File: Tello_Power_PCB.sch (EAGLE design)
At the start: 134 parts, among them CON1 XT30PW-F, CON2 XT30PW-F, CON3 XT30PW-F, CON4 XT30PW-F, CON7 XT60PW-M, J1 PJ-002A, J10 SM02BGHSTBLFSN, J2 1719740002, J3 1719740002, J4 1719740002, J5 1719740002, J6 1719740002, J7 1719740002, J8 1719740002, J9 1719740002, M1 30V, M2 60V, M3 30V, M4 60V, Q1 BSC027N06LS5ATMA1, Q2 BSC027N06LS5ATMA1, Q3 IXTA96P085T, Q7 IXTA96P085T, Q8 IXTA96P085T, Q9 IXTA96P085T, U1 LM3150MH/NOPB, U10 TLV6713DDCTDDC0006A_M, U11 TLV6713DDCTDDC0006A_M, U12 DMN67D8LW-13, U13 MCP1792T-5002H/CB, U14 TLV6713DDCTDDC0006A_M, U2 LM3150MH/NOPB, U3 LTC4357CMS8TRPBF, U4 ADS1015IDGST, U5 DMN67D8LW-13, U6 DMN67D8LW-13, U7 DMN67D8LW-13, U8 LTC4357CMS8TRPBF, U9 TLV6713DDCTDDC0006A_M

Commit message: Organized Schematic
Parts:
- R20, R21: value (none) -> 100K
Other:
- note added: "Battery Input"
- note added: "I²C Address is 1001000"
- note removed: "Default I²C Address = 1001000"
- note removed: "Power Input"

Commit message: Review Finished
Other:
- note removed: "ADD BULK CAPACITANCE HERE"
- note removed: "Bulk capacitance shown on the other Reg. circuit"
- moved on the sheet: C10, C11, C12, C13, C14, C15, C16, C17, C18, C19, C20, C21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

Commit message: Added mfg files and renders
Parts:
- C1, C2, C29, C36, C38: device rcl:C-EUC1206 -> Tello_Power_PCB:RCL_C-EUC1206
- C10, C9: device 12v- LM3150:C2012X5R1V156M125AC -> Tello_Power_PCB:12V--LM3150_C2012X5R1V156M125AC
- C11: device 12v- LM3150:C1005X5R1H104K050BB -> Tello_Power_PCB:12V--LM3150_C1005X5R1H104K050BB
- C12, C24: device CGA4F2C0G1H153J085AA:CGA4F2C0G1H153J085AA -> Tello_Power_PCB:CGA4F2C0G1H153J085AA_CGA4F2C0G1H153J085AA
- C13: device 12v- LM3150:EMK212BJ225KG-T -> Tello_Power_PCB:12V--LM3150_EMK212BJ225KG-T:1
- C14: device 12v- LM3150:ECPU1C474MA5 -> Tello_Power_PCB:12V--LM3150_ECPU1C474MA5:1
- C15: device 12v- LM3150:C0805C301J5GACTU -> Tello_Power_PCB:12V--LM3150_C0805C301J5GACTU
- C16: device 12v- LM3150:PCV1E330MCL1GS -> Tello_Power_PCB:12V--LM3150_PCV1E330MCL1GS
- C17, C18, C19, C4, C5, C6: value PCR1H820MCL1GS -> PCR1H820MCL1GS_PCR1H820MCL1GS; device PCR1H820MCL1GS:PCR1H820MCL1GS -> Tello_Power_PCB:PCR1H820MCL1GS_PCR1H820MCL1GS
- C20: device 5v-LM3150MH:293D335X9035C2TE3 -> Tello_Power_PCB:5V-LM3150MH_293D335X9035C2TE3
- C21, C22: device 5v-LM3150MH:C2012X5R1V106K085AC -> Tello_Power_PCB:5V-LM3150MH_C2012X5R1V106K085AC
- C23: device 5v-LM3150MH:CGA3E2X7R1H104K080AA -> Tello_Power_PCB:5V-LM3150MH_CGA3E2X7R1H104K080AA
- C25: device 5v-LM3150MH:EMK212BJ225KG-T -> Tello_Power_PCB:5V-LM3150MH_EMK212BJ225KG-T
- C26: device 5v-LM3150MH:ECPU1C474MA5 -> Tello_Power_PCB:5V-LM3150MH_ECPU1C474MA5
- C27: device 5v-LM3150MH:CL21C620JBANNNC -> Tello_Power_PCB:5V-LM3150MH_CL21C620JBANNNC
- C28: device 5v-LM3150MH:CUSTOM_CAP -> Tello_Power_PCB:5V-LM3150MH_CUSTOM_CAP
- C3, C30, C37: device rcl:C-EUC0603 -> Tello_Power_PCB:RCL_C-EUC0603
- C31, C32, C33, C34, C35: value 227AVG050MGBJ -> 227AVG050MGBJ_227AVG050MGBJ; device 227AVG050MGBJ:227AVG050MGBJ -> Tello_Power_PCB:227AVG050MGBJ_227AVG050MGBJ
- C39: device microbuilder:CAP_CERAMIC0603 -> Tello_Power_PCB:MICROBUILDER_CAP_CERAMIC0603
- C40, C41: device rcl:C-EUC1210 -> Tello_Power_PCB:RCL_C-EUC1210
- C7, C8: device 12v- LM3150:TPSB475K035R0700 -> Tello_Power_PCB:12V--LM3150_TPSB475K035R0700
- CON1, CON2, CON3, CON4: value XT30PW-F -> AMASS_XT30PW-F; device amass:XT30PW-F -> Tello_Power_PCB:AMASS_XT30PW-F
- CON7: value XT60PW-M -> AMASS_XT60PW-M; device amass:XT60PW-M -> Tello_Power_PCB:AMASS_XT60PW-M
- CR1, CR2: value STPS1150A -> STPS1150A_STPS1150A; device STPS1150A:STPS1150A -> Tello_Power_PCB:STPS1150A_STPS1150A
- J1: value PJ-002A -> PJ-002A_PJ-002A; device PJ-002A:PJ-002A -> Tello_Power_PCB:PJ-002A_PJ-002A
- J10: value SM02BGHSTBLFSN -> SM02B-GHS-TB_SM02BGHSTBLFSN; device SM02B-GHS-TB:SM02BGHSTBLFSN -> Tello_Power_PCB:SM02B-GHS-TB_SM02BGHSTBLFSN
- J2, J3, J4, J5, J6, J7, J8, J9: value 1719740002 -> 1719740002_1719740002; device 1719740002:1719740002 -> Tello_Power_PCB:1719740002_1719740002
- JP1: device pinhead:PINHD-2X6 -> Tello_Power_PCB:PINHEAD_PINHD-2X6
- JP2: value JUMPER-SMT_2_NC_PASTE_NO-SILK -> SPARKFUN-JUMPERS_JUMPER-SMT_2_NC_PASTE_NO-SILK; device SparkFun-Jumpers:JUMPER-SMT_2_NC_PASTE_NO-SILK -> Tello_Power_PCB:SPARKFUN-JUMPERS_JUMPER-SMT_2_NC_PASTE_NO-SILK
- L1: device 12v- LM3150:74437358082 -> Tello_Power_PCB:12V--LM3150_74437358082
- L2: device 5v-LM3150MH:XAL5030-222MEB -> Tello_Power_PCB:5V-LM3150MH_XAL5030-222MEB
- L3: device XAL4030-332MEB:XAL4030-332MEB -> Tello_Power_PCB:XAL4030-332MEB_XAL4030-332MEB
- L4: device 5v-LM3150MH:NPI43C3R9MTRF -> Tello_Power_PCB:5V-LM3150MH_NPI43C3R9MTRF
- LED1, LED2, LED3, LED4: device led:LEDCHIP-LED0603 -> Tello_Power_PCB:LED_LEDCHIP-LED0603
- M1: device 12v- LM3150:CSD17579Q5A -> Tello_Power_PCB:12V--LM3150_CSD17579Q5A:1
- M2: device 12v- LM3150:CSD18537NQ5A -> Tello_Power_PCB:12V--LM3150_CSD18537NQ5A:1
- M3: device 5v-LM3150MH:CSD17579Q5A -> Tello_Power_PCB:5V-LM3150MH_CSD17579Q5A
- M4: device 5v-LM3150MH:CSD18537NQ5A -> Tello_Power_PCB:5V-LM3150MH_CSD18537NQ5A
- Q1, Q2: value BSC027N06LS5ATMA1 -> BSC027N06LS5ATMA1_BSC027N06LS5ATMA1; device BSC027N06LS5ATMA1:BSC027N06LS5ATMA1 -> Tello_Power_PCB:BSC027N06LS5ATMA1_BSC027N06LS5ATMA1
- Q3, Q7, Q8, Q9: value IXTA96P085T -> IXTA96P085T_IXTA96P085T; device IXTA96P085T:IXTA96P085T -> Tello_Power_PCB:IXTA96P085T_IXTA96P085T
- R1: device 12v- LM3150:CRCW04021R00FKED -> Tello_Power_PCB:12V--LM3150_CRCW04021R00FKED
- R10: device 5v-LM3150MH:CRCW080510K0FKEA -> Tello_Power_PCB:5V-LM3150MH_CRCW080510K0FKEA
- R11: device rcl:R-US_R0805 -> Tello_Power_PCB:RCL_R-US_R0805
- R12, R13, R14, R15, R16, R19, R20, R21, R22, R25, R27, R28, R29, R30, R38, R39, R40, R41, R42, R5: device rcl:R-US_R0603 -> Tello_Power_PCB:RCL_R-US_R0603
- R17, R18, R4: value 68XR10KLF -> 68XR10KLF_68XR10KLF; device 68XR10KLF:68XR10KLF -> Tello_Power_PCB:68XR10KLF_68XR10KLF
- R2: device 12v- LM3150:ERJ-6ENF3323V -> Tello_Power_PCB:12V--LM3150_ERJ-6ENF3323V
- R23, R24, R26, R31, R32, R33, R34, R35, R36, R37: device microbuilder:RESISTOR0603 -> Tello_Power_PCB:MICROBUILDER_RESISTOR0603
- R3: device 12v- LM3150:ERJ-6ENF1371V -> Tello_Power_PCB:12V--LM3150_ERJ-6ENF1371V
- R6: device 5v-LM3150MH:ERJ-3RSFR10V -> Tello_Power_PCB:5V-LM3150MH_ERJ-3RSFR10V
- R7: device 5v-LM3150MH:ERJ-6ENF5112V -> Tello_Power_PCB:5V-LM3150MH_ERJ-6ENF5112V
- R8: device 5v-LM3150MH:ERJ-6ENF1581V -> Tello_Power_PCB:5V-LM3150MH_ERJ-6ENF1581V
- R9: device 5v-LM3150MH:CRCW080573K2FKEA -> Tello_Power_PCB:5V-LM3150MH_CRCW080573K2FKEA
- U1, U2: value LM3150MH/NOPB -> 5V-LM3150MH_LM3150MH/NOPB; device 5v-LM3150MH:LM3150MH/NOPB -> Tello_Power_PCB:5V-LM3150MH_LM3150MH/NOPB
- U10, U11, U14, U9: value TLV6713DDCTDDC0006A_M -> TLV6713DDC_TLV6713DDCTDDC0006A_M; device TLV6713DDC:TLV6713DDCTDDC0006A_M -> Tello_Power_PCB:TLV6713DDC_TLV6713DDCTDDC0006A_M
- U12, U5, U6, U7: value DMN67D8LW-13 -> DMN67D8LW-13_DMN67D8LW-13; device DMN67D8LW-13:DMN67D8LW-13 -> Tello_Power_PCB:DMN67D8LW-13_DMN67D8LW-13
- U13: value MCP1792T-5002H/CB -> MCP1792T-5002H_MCP1792T-5002H/CB; device MCP1792T-5002H:MCP1792T-5002H/CB -> Tello_Power_PCB:MCP1792T-5002H_MCP1792T-5002H/CB
- U3, U8: value LTC4357CMS8TRPBF -> LTC4357_LTC4357CMS8TRPBF; device LTC4357:LTC4357CMS8TRPBF -> Tello_Power_PCB:LTC4357_LTC4357CMS8TRPBF
- U4: device microbuilder:ADC_ADS1015 -> Tello_Power_PCB:MICROBUILDER_ADC_ADS1015

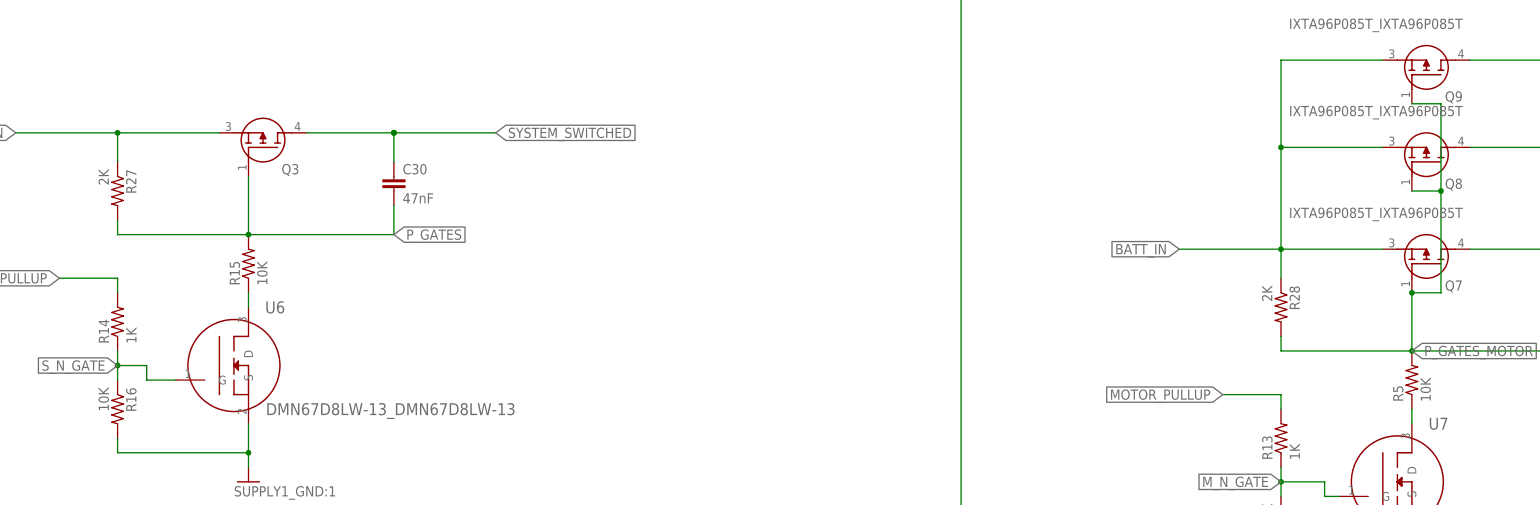
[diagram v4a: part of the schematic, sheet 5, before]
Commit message: updated readme photos
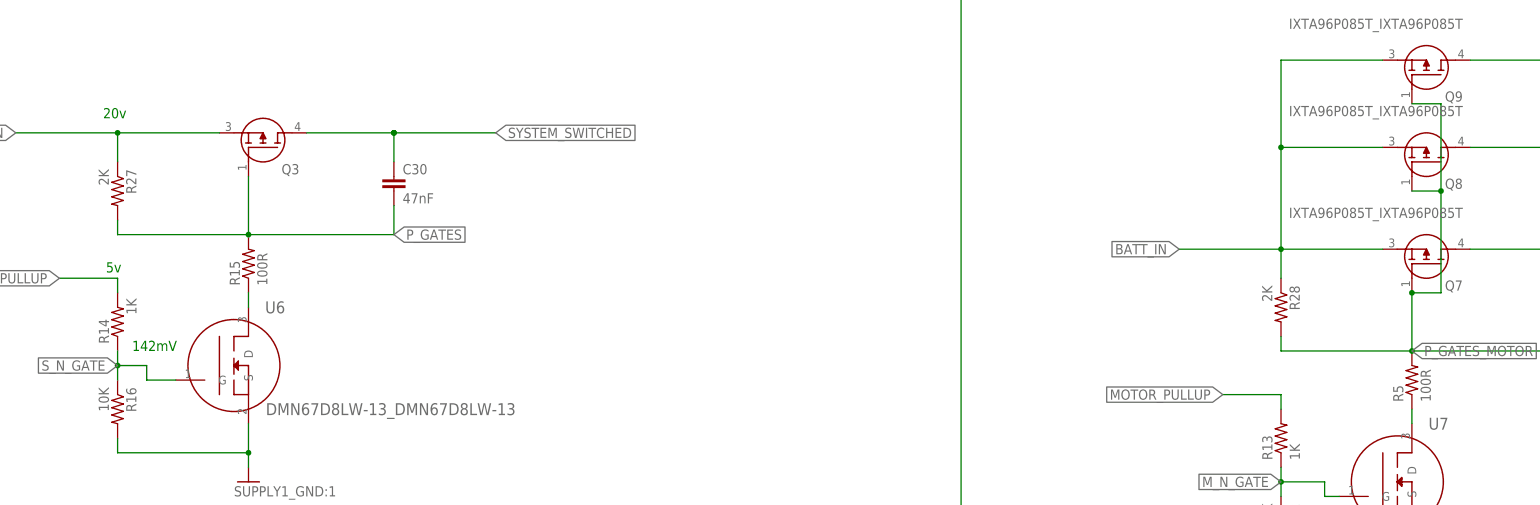
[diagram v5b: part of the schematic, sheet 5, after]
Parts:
- R15, R5: value 10K -> 100R
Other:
- note added: "142mV"
- note added: "20v"
- note added: "3.89v?"
- note added: "4.77"
- note added: "5.24v"
- note added: "5v"
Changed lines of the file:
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@@
 <part name="Q3" library="Tello_Power_PCB" library_urn="urn:adsk.eagle:library:37573195" deviceset="IXTA96P085T_IXTA96P085T" device="" package3d_urn="urn:adsk.eagle:package:37573289/3"/>
 <part name="R27" library="Tello_Power_PCB" library_urn="urn:adsk.eagle:library:37573195" deviceset="RCL_R-US_" device="R0603" package3d_urn="urn:adsk.eagle:package:37573323/1" value="2K"/>
-<part name="R15" library="Tello_Power_PCB" library_urn="urn:adsk.eagle:library:37573195" deviceset="RCL_R-US_" device="R0603" package3d_urn="urn:adsk.eagle:package:37573323/1" value="10K"/>
+<part name="R15" library="Tello_Power_PCB" library_urn="urn:adsk.eagle:library:37573195" deviceset="RCL_R-US_" device="R0603" package3d_urn="urn:adsk.eagle:package:37573323/1" value="100R"/>
 <part name="GND14" library="Tello_Power_PCB" library_urn="urn:adsk.eagle:library:37573195" deviceset="SUPPLY1_GND*?:1" device=""/>
 <part name="R16" library="Tello_Power_PCB" library_urn="urn:adsk.eagle:library:37573195" deviceset="RCL_R-US_" device="R0603" package3d_urn="urn:adsk.eagle:package:37573323/1" value="10K"/>
@@
 <part name="Q9" library="Tello_Power_PCB" library_urn="urn:adsk.eagle:library:37573195" deviceset="IXTA96P085T_IXTA96P085T" device="" package3d_urn="urn:adsk.eagle:package:37573289/3"/>
 <part name="C3" library="Tello_Power_PCB" library_urn="urn:adsk.eagle:library:37573195" deviceset="RCL_C-EU" device="C0603" package3d_urn="urn:adsk.eagle:package:37573320/1" value="47nF"/>
-<part name="R5" library="Tello_Power_PCB" library_urn="urn:adsk.eagle:library:37573195" deviceset="RCL_R-US_" device="R0603" package3d_urn="urn:adsk.eagle:package:37573323/1" value="10K"/>
+<part name="R5" library="Tello_Power_PCB" library_urn="urn:adsk.eagle:library:37573195" deviceset="RCL_R-US_" device="R0603" package3d_urn="urn:adsk.eagle:package:37573323/1" value="100R"/>
 <part name="FRAME11" library="Tello_Power_PCB" library_urn="urn:adsk.eagle:library:37573195" deviceset="FRAMES_FRAME_A_L" device=""/>
 <part name="FRAME12" library="Tello_Power_PCB" library_urn="urn:adsk.eagle:library:37573195" deviceset="FRAMES_FRAME_B_L" device=""/>
@@
 <text x="233.934" y="187.96" size="12.7" layer="91">Motor High Side Switch</text>
 <text x="233.934" y="172.72" size="7.62" layer="91">With Inrush Current Limiter</text>
+<text x="66.04" y="144.78" size="1.778" layer="91">20v</text>
+<text x="71.12" y="104.14" size="1.778" layer="91">142mV</text>
+<text x="66.548" y="117.856" size="1.778" layer="91">5v</text>
 </plain>
 <instances>
@@
 <instance part="R14" gate="G$1" x="68.58" y="109.22" smashed="yes" rot="R90">
 <attribute name="NAME" x="67.0814" y="105.41" size="1.778" layer="95" rot="R90"/>
-<attribute name="VALUE" x="71.882" y="105.41" size="1.778" layer="96" rot="R90"/>
+<attribute name="VALUE" x="71.882" y="110.49" size="1.778" layer="96" rot="R90"/>
 </instance>
 <instance part="Q7" gate="G$1" x="294.64" y="114.3" smashed="yes" rot="MR90">
@@
 <text x="15.24" y="256.54" size="6.35" layer="91">Under- Voltage Protection Circuitry</text>
 <text x="261.62" y="157.48" size="2.54" layer="91">30 Second Filter Circuit</text>
+<text x="312.42" y="91.44" size="1.778" layer="91">5v</text>
+<text x="287.02" y="78.74" size="1.778" layer="91">3.89v?</text>
+<text x="233.68" y="91.44" size="1.778" layer="91">5.24v</text>
+<text x="322.58" y="83.82" size="1.778" layer="91">4.77</text>
 </plain>
 <instances>

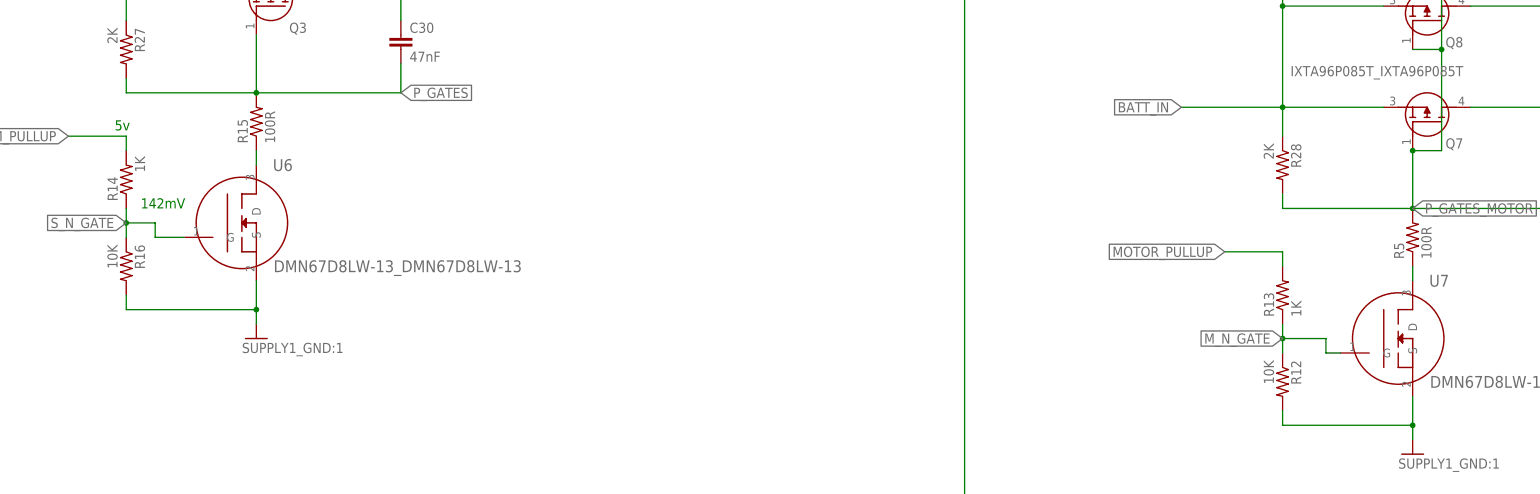
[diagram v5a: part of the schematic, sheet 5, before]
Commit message: updated high side switch resistors
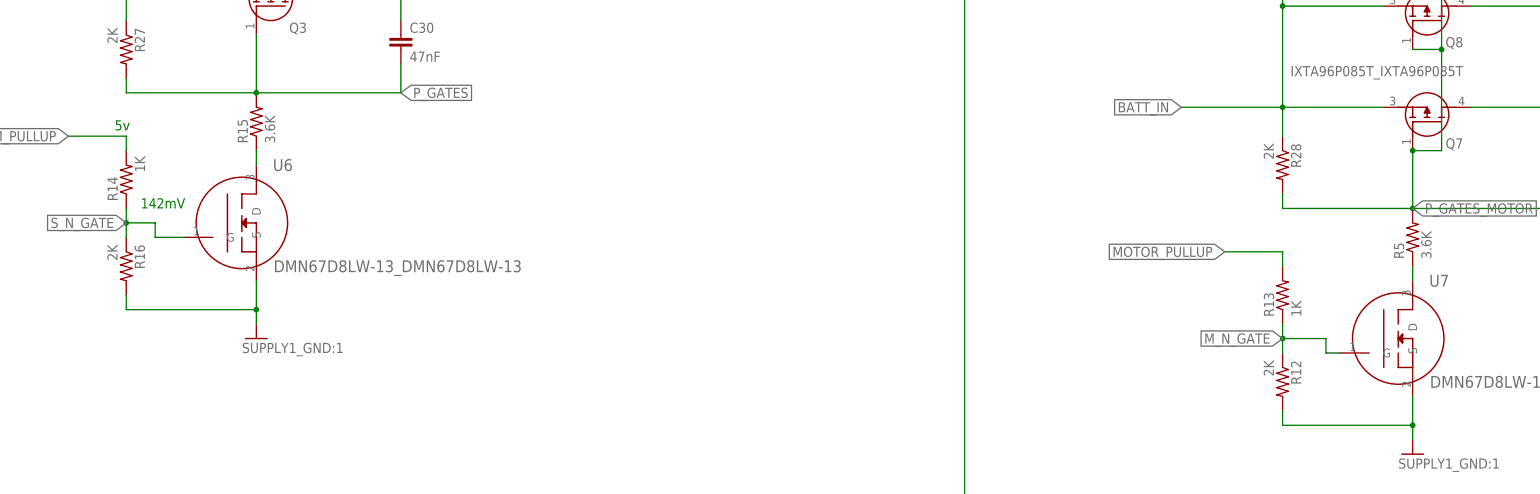
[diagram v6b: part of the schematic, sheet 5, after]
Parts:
- R12, R16: value 10K -> 2K
- R15, R5: value 100R -> 3.6K
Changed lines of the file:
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@@
 <part name="Q3" library="Tello_Power_PCB" library_urn="urn:adsk.eagle:library:37573195" deviceset="IXTA96P085T_IXTA96P085T" device="" package3d_urn="urn:adsk.eagle:package:37573289/3"/>
 <part name="R27" library="Tello_Power_PCB" library_urn="urn:adsk.eagle:library:37573195" deviceset="RCL_R-US_" device="R0603" package3d_urn="urn:adsk.eagle:package:37573323/1" value="2K"/>
-<part name="R15" library="Tello_Power_PCB" library_urn="urn:adsk.eagle:library:37573195" deviceset="RCL_R-US_" device="R0603" package3d_urn="urn:adsk.eagle:package:37573323/1" value="100R"/>
+<part name="R15" library="Tello_Power_PCB" library_urn="urn:adsk.eagle:library:37573195" deviceset="RCL_R-US_" device="R0603" package3d_urn="urn:adsk.eagle:package:37573323/1" value="3.6K"/>
 <part name="GND14" library="Tello_Power_PCB" library_urn="urn:adsk.eagle:library:37573195" deviceset="SUPPLY1_GND*?:1" device=""/>
-<part name="R16" library="Tello_Power_PCB" library_urn="urn:adsk.eagle:library:37573195" deviceset="RCL_R-US_" device="R0603" package3d_urn="urn:adsk.eagle:package:37573323/1" value="10K"/>
+<part name="R16" library="Tello_Power_PCB" library_urn="urn:adsk.eagle:library:37573195" deviceset="RCL_R-US_" device="R0603" package3d_urn="urn:adsk.eagle:package:37573323/1" value="2K"/>
 <part name="R14" library="Tello_Power_PCB" library_urn="urn:adsk.eagle:library:37573195" deviceset="RCL_R-US_" device="R0603" package3d_urn="urn:adsk.eagle:package:37573323/1" value="1K"/>
 <part name="C31" library="Tello_Power_PCB" library_urn="urn:adsk.eagle:library:37573195" deviceset="227AVG050MGBJ_227AVG050MGBJ" device="" package3d_urn="urn:adsk.eagle:package:37573294/4"/>
@@
 <part name="R28" library="Tello_Power_PCB" library_urn="urn:adsk.eagle:library:37573195" deviceset="RCL_R-US_" device="R0603" package3d_urn="urn:adsk.eagle:package:37573323/1" value="2K"/>
 <part name="GND13" library="Tello_Power_PCB" library_urn="urn:adsk.eagle:library:37573195" deviceset="SUPPLY1_GND*?:1" device=""/>
-<part name="R12" library="Tello_Power_PCB" library_urn="urn:adsk.eagle:library:37573195" deviceset="RCL_R-US_" device="R0603" package3d_urn="urn:adsk.eagle:package:37573323/1" value="10K"/>
+<part name="R12" library="Tello_Power_PCB" library_urn="urn:adsk.eagle:library:37573195" deviceset="RCL_R-US_" device="R0603" package3d_urn="urn:adsk.eagle:package:37573323/1" value="2K"/>
 <part name="R13" library="Tello_Power_PCB" library_urn="urn:adsk.eagle:library:37573195" deviceset="RCL_R-US_" device="R0603" package3d_urn="urn:adsk.eagle:package:37573323/1" value="1K"/>
 <part name="Q9" library="Tello_Power_PCB" library_urn="urn:adsk.eagle:library:37573195" deviceset="IXTA96P085T_IXTA96P085T" device="" package3d_urn="urn:adsk.eagle:package:37573289/3"/>
 <part name="C3" library="Tello_Power_PCB" library_urn="urn:adsk.eagle:library:37573195" deviceset="RCL_C-EU" device="C0603" package3d_urn="urn:adsk.eagle:package:37573320/1" value="47nF"/>
-<part name="R5" library="Tello_Power_PCB" library_urn="urn:adsk.eagle:library:37573195" deviceset="RCL_R-US_" device="R0603" package3d_urn="urn:adsk.eagle:package:37573323/1" value="100R"/>
+<part name="R5" library="Tello_Power_PCB" library_urn="urn:adsk.eagle:library:37573195" deviceset="RCL_R-US_" device="R0603" package3d_urn="urn:adsk.eagle:package:37573323/1" value="3.6K"/>
 <part name="FRAME11" library="Tello_Power_PCB" library_urn="urn:adsk.eagle:library:37573195" deviceset="FRAMES_FRAME_A_L" device=""/>
 <part name="FRAME12" library="Tello_Power_PCB" library_urn="urn:adsk.eagle:library:37573195" deviceset="FRAMES_FRAME_B_L" device=""/>
